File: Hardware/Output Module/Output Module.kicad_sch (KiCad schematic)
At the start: 16 parts, among them J1 Conn_01x12_Male, J2 Conn_01x03_Male, J3 Screw_Terminal_01x02, J4 Screw_Terminal_01x08, Q1 NCV8403A, Q2 NCV8403A, Q3 NCV8403A, Q4 NCV8403A

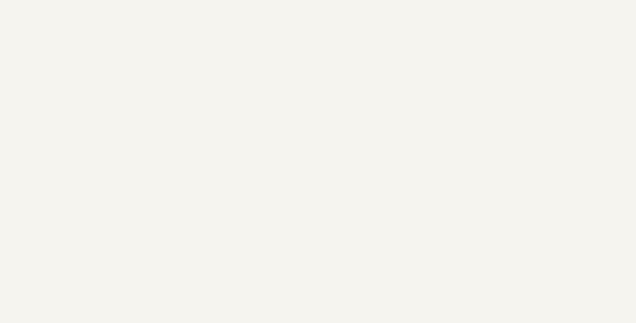
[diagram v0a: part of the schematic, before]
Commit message: update footprints, cad model for plastic clip
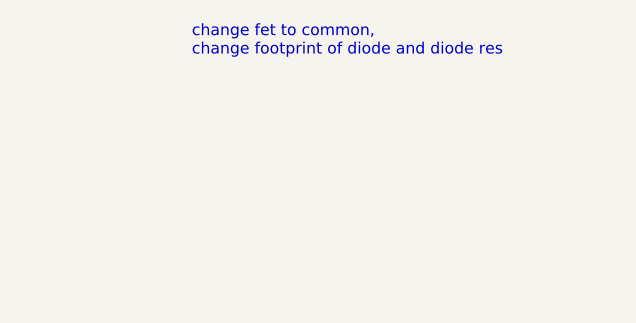
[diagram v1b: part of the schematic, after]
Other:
- note added: "change fet to common, change footprint of diode and diode res"
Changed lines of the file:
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@@
     (stroke (width 0) (type default) (color 0 0 0 0))
+  )
+  (text "change fet to common,\nchange footprint of diode and diode res"
+    (at 308.61 20.32 0)
+    (effects (font (size 1.27 1.27)) (justify left bottom))
   )
   (text "Vmot" (at 114.3 43.18 0)
@@
     )
     (pin "1")
-    (pin "4")
-    (pin "3")
+    (pin "3")
+    (pin "4")
   )
   (symbol (lib_id "Device:R_Small") (at 119.38 86.36 0) (unit 1)

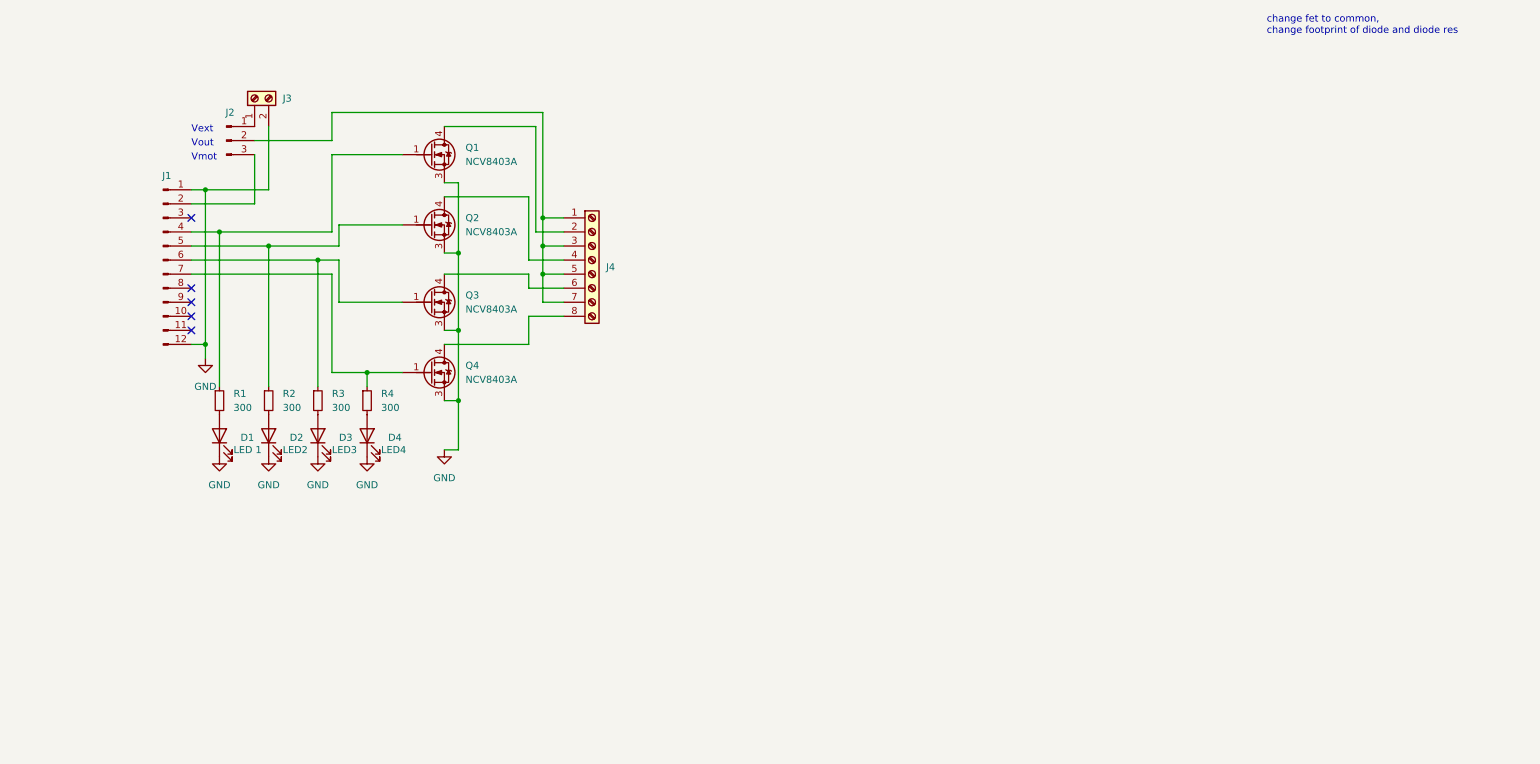
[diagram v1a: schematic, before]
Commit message: redesigned input and output modules, cleaned some files, ordered 10 of each
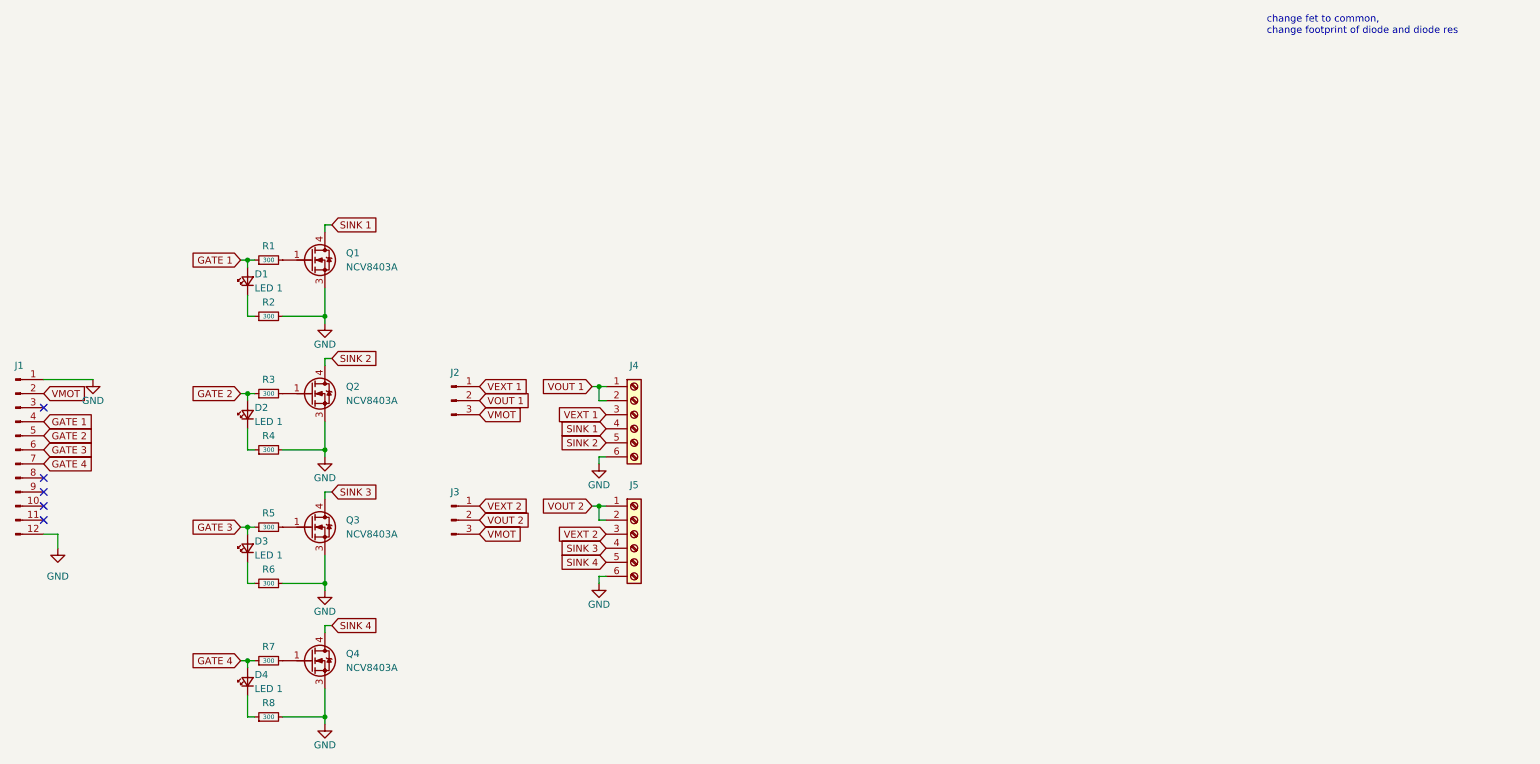
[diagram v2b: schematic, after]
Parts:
- removed D1: LED 1, LED_SMD:LED_0603_1608Metric_Pad1.05x0.95mm_HandSolder, symbol Device:LED
- removed D2: LED2, LED_SMD:LED_0603_1608Metric_Pad1.05x0.95mm_HandSolder, symbol Device:LED
- removed D3: LED3, LED_SMD:LED_0603_1608Metric_Pad1.05x0.95mm_HandSolder, symbol Device:LED
- removed D4: LED4, LED_SMD:LED_0603_1608Metric_Pad1.05x0.95mm_HandSolder, symbol Device:LED
- removed J3: Screw_Terminal_01x02, TerminalBlock_Phoenix:TerminalBlock_Phoenix_MKDS-1,5-2-5.08_1x02_P5.08mm_Horizontal, symbol Connector:Screw_Terminal_01x02
- removed J4: Screw_Terminal_01x08, TerminalBlock_Phoenix:TerminalBlock_Phoenix_PT-1,5-8-3.5-H_1x08_P3.50mm_Horizontal, symbol Connector:Screw_Terminal_01x08
- added D1, D2, D3, D4: LED 1, LED_SMD:LED_0603_1608Metric, symbol Device:LED_Small
- added J3: Conn_01x03_Male, Connector_PinHeader_2.54mm:PinHeader_1x03_P2.54mm_Vertical, symbol Connector:Conn_01x03_Male
- added J4, J5: Screw_Terminal_01x06, KiCad:2x3 screw terminal3.5mm, symbol Connector:Screw_Terminal_01x06
- added R5, R6, R7, R8: 300, Resistor_SMD:R_0603_1608Metric, symbol Device:R_Small
- R1, R2, R3, R4: footprint Resistor_SMD:R_0201_0603Metric_Pad0.64x0.40mm_HandSolder -> Resistor_SMD:R_0603_1608Metric
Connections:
- net GND: now also R2.2, R4.2, J4.6 (Pin_6), J5.6 (Pin_6), R6.2, R8.2
- net VEXT 1: now reaches J2.1 (Pin_1)
- net VEXT 1: now also J4.3 (Pin_3)
- net VOUT 1: now reaches J2.2 (Pin_2)
- net VOUT 1: now also J4.1 (Pin_1), J4.2 (Pin_2)
- net VMOT: now reaches J1.2 (Pin_2), J2.3 (Pin_3)
- net VMOT: now also J3.3 (Pin_3)
- net at R1.2: now also Q1.1 (G)
- net at R3.2: now also Q2.1 (G)
- net SINK 4: now reaches Q4.4 (D)
- net SINK 4: now also J5.5 (Pin_5)
- net GATE 1: now reaches J1.4 (Pin_4), R1.1
- net GATE 1: now also D1.2 (A); no longer Q1.1 (G)
- net SINK 1: now reaches Q1.4 (D)
- net SINK 1: now also J4.4 (Pin_4)
- net SINK 2: now reaches Q2.4 (D)
- net SINK 2: now also J4.5 (Pin_5)
- net SINK 3: now reaches Q3.4 (D)
- net SINK 3: now also J5.4 (Pin_4)
- new net: Q3.1 (G), R5.2
- new net: D1.1 (K), R2.1
- new net: D2.1 (K), R4.1
- new net: D3.1 (K), R6.1
- new net: Q4.1 (G), R7.2
- new net: D4.1 (K), R8.1
- new net GATE 2: D2.2 (A), J1.5 (Pin_5), R3.1
- new net GATE 3: D3.2 (A), J1.6 (Pin_6), R5.1
- new net GATE 4: D4.2 (A), J1.7 (Pin_7), R7.1
- new net VEXT 2: J3.1 (Pin_1), J5.3 (Pin_3)
- new net VOUT 2: J3.2 (Pin_2), J5.1 (Pin_1), J5.2 (Pin_2)
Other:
- note removed: "Vext"
- note removed: "Vmot"
- note removed: "Vout"
- company: (none) -> Torban Consulting
- title: (none) -> Quad Output Module for 6-Pack
- moved on the sheet: J1, J2, Q1
